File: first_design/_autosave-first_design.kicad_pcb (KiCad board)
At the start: 2 copper layers, 65 x 56.5 mm, 43 parts, among them IC1 BD48K60, IC2 AZ2085D-ADJTRG1, IC3 AP65450, IC5 VNH7070BAS, J1 Conn_02x20_Odd_Even, J2 Conn_01x02, J3 Accelerometer_standard, J4 Servo_motor, J5 Battery, Q1 2N7002K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

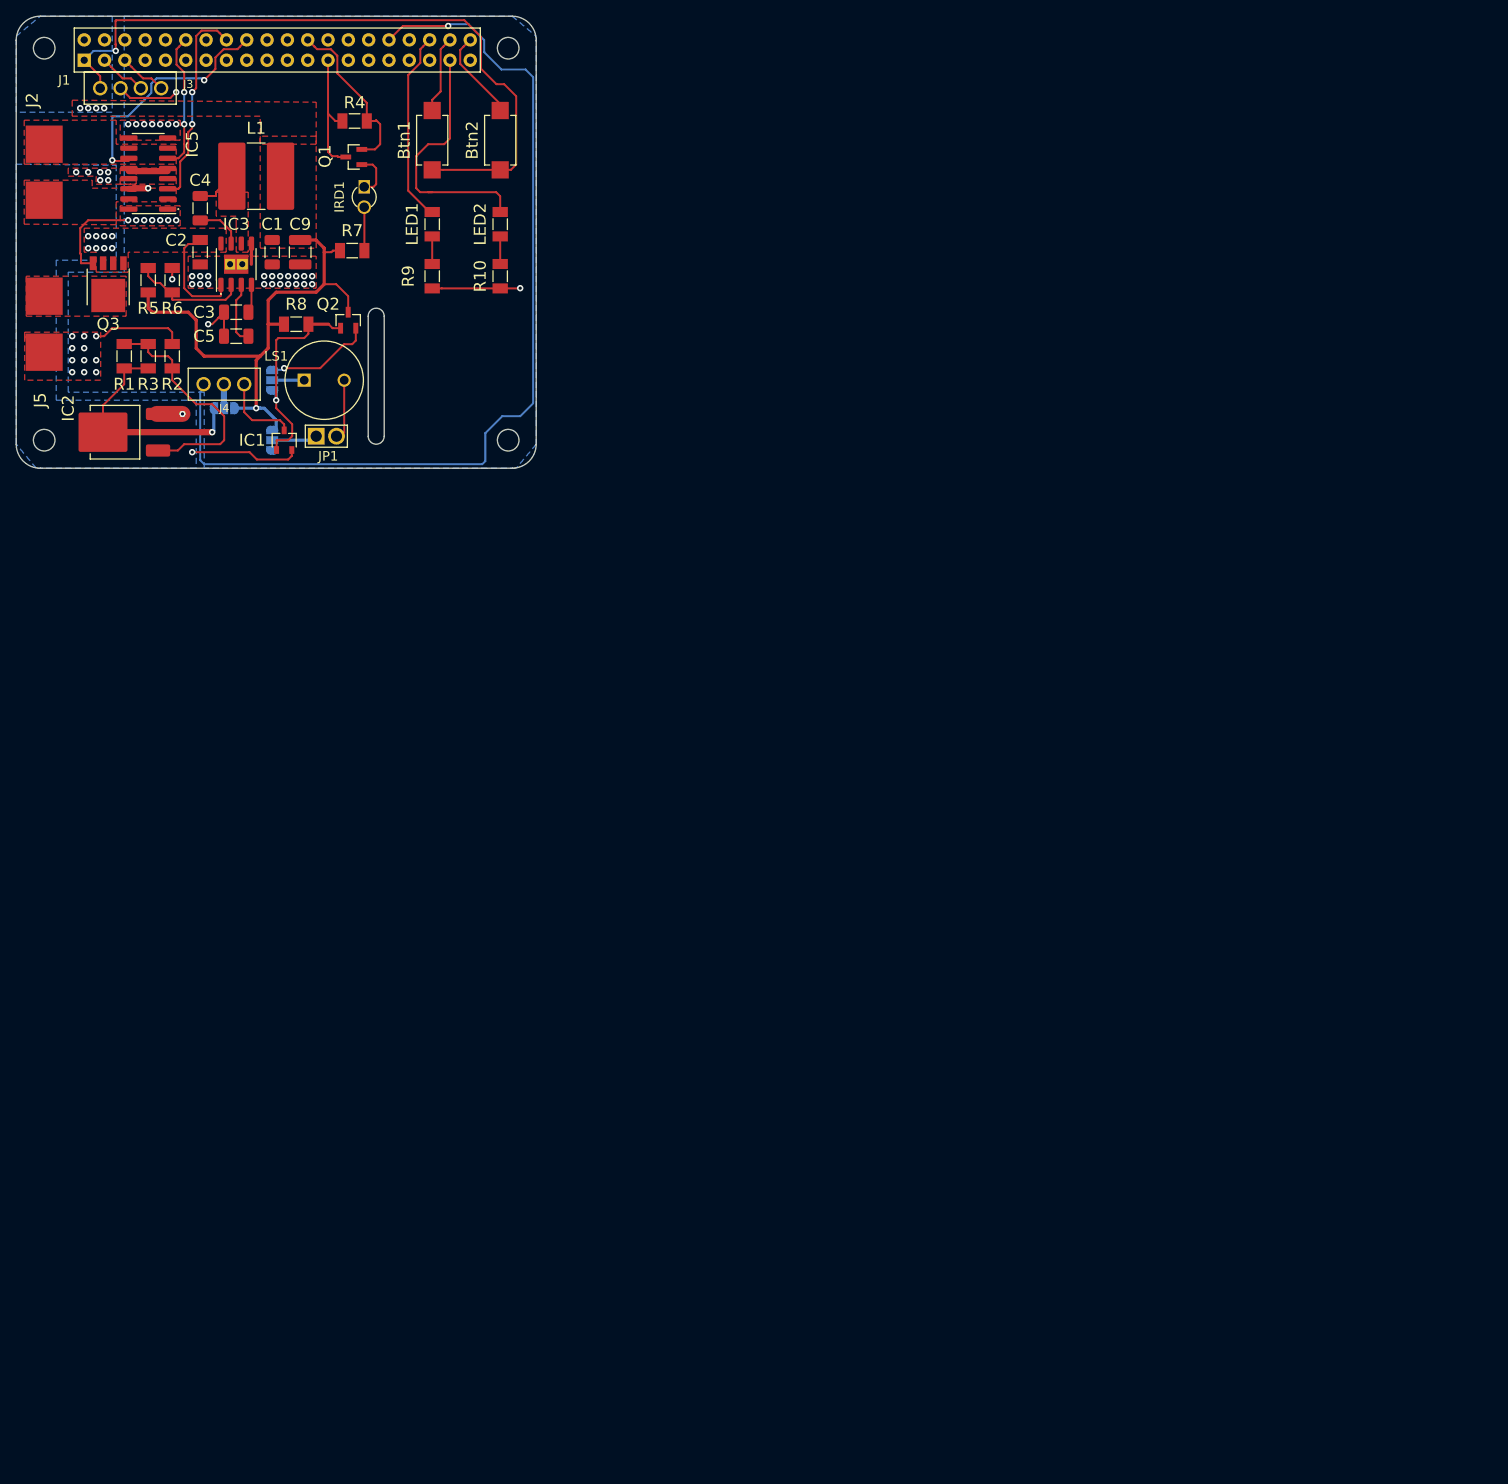
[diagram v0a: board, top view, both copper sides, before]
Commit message: Remove extra components after playing with the first prototype
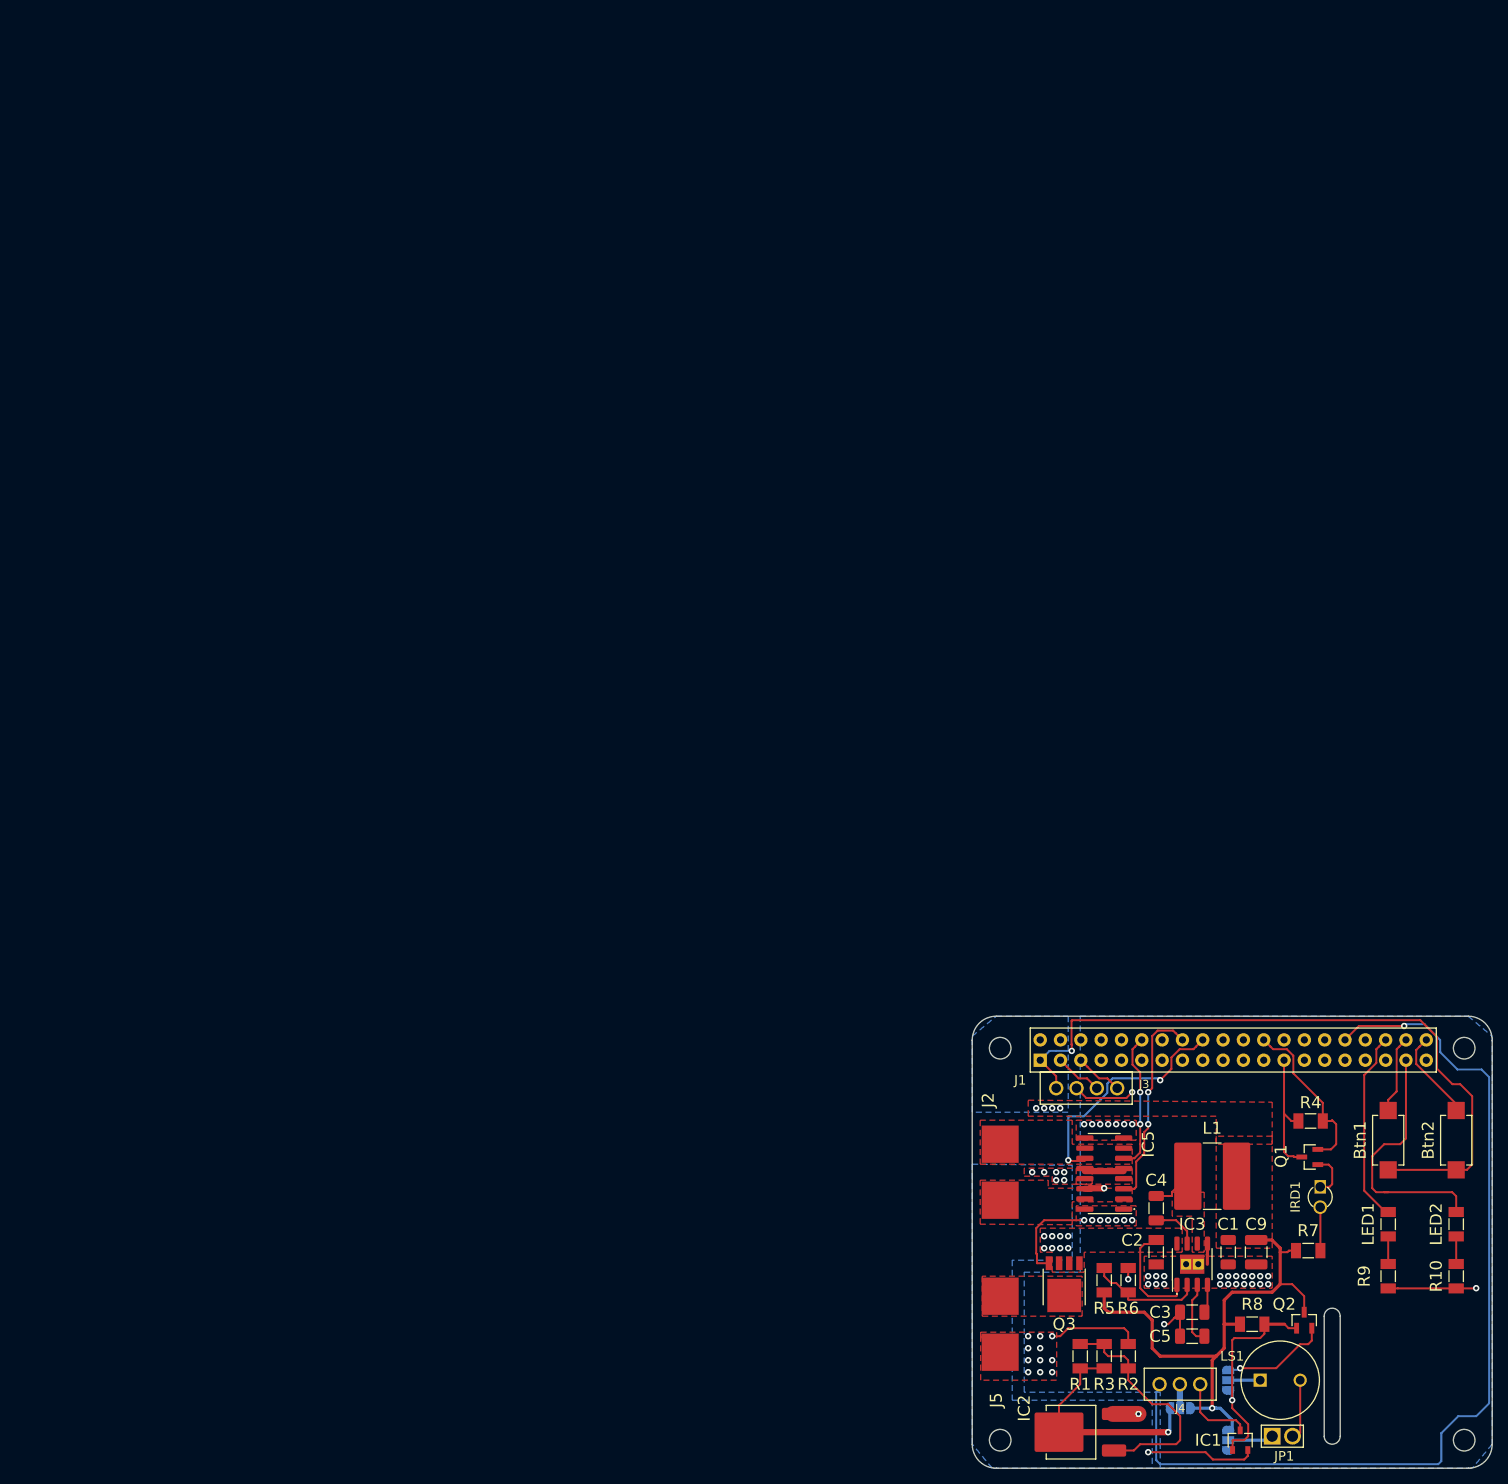
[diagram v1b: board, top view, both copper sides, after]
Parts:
- moved Btn1 172.9 mm to (171.5, 84.0)
- moved Btn2 172.9 mm to (180.0, 84.0)
- moved C1 172.9 mm to (151.5, 98.0)
- moved C2 172.9 mm to (142.5, 98.0)
- moved C3 172.9 mm to (147.0, 105.5)
- moved C4 172.9 mm to (142.5, 92.5)
- moved C5 172.9 mm to (147.0, 108.5)
- moved C9 172.9 mm to (155.0, 98.0)
- moved H1 172.9 mm to (123.0, 72.5)
- moved H2 172.9 mm to (181.0, 72.5)
- moved H3 172.9 mm to (123.0, 121.5)
- moved H4 172.9 mm to (181.0, 121.5)
- moved IC1 172.9 mm to (153.0, 121.5)
- moved IC2 172.9 mm to (133.0, 120.5)
- moved IC3 172.9 mm to (147.0, 99.5)
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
